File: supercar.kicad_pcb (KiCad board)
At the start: 2 copper layers, 63.5 x 48.9 mm, 59 parts, among them SW1 Power, U1 74HC283, U2 74HC574, U3 74HC154, U4 74HC574, U5 74HC21, U6 74HC02, U7 74HC04, U8 NE555D

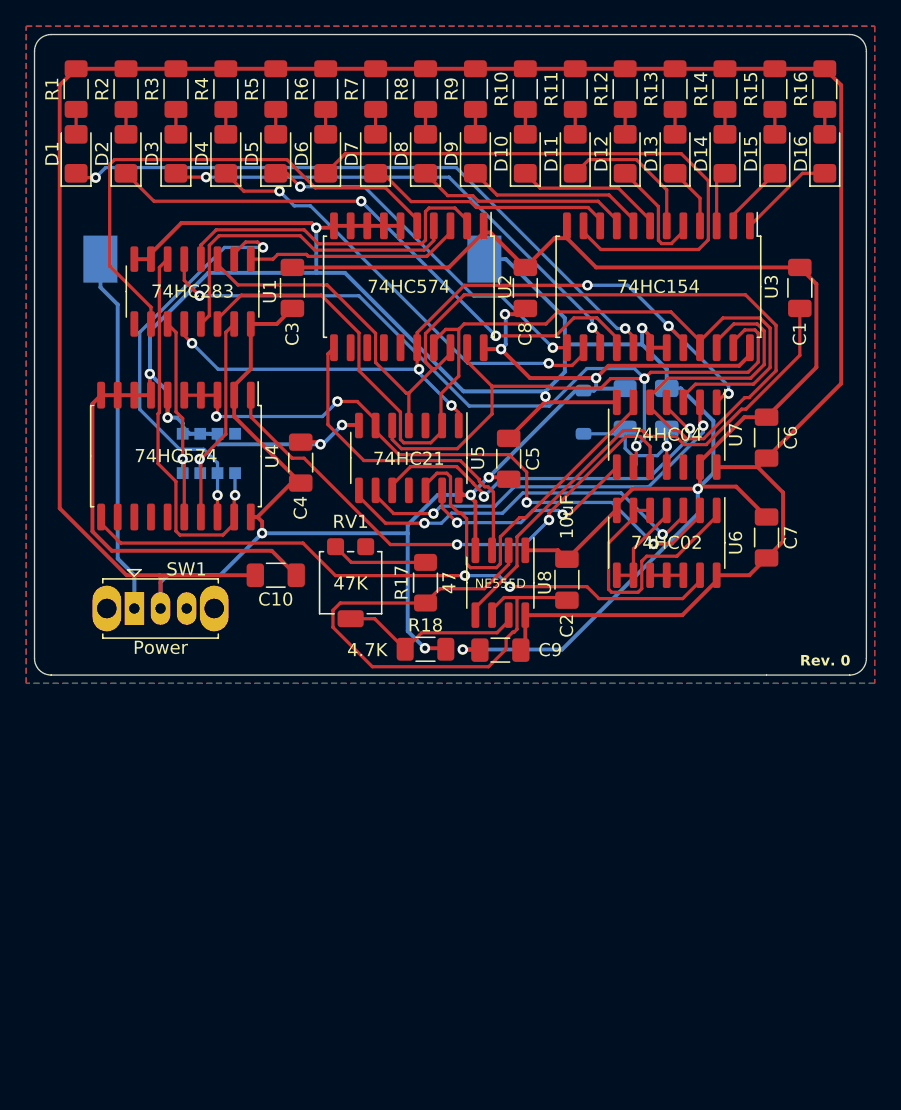
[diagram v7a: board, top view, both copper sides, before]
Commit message: Reduce IC count and reroute the board
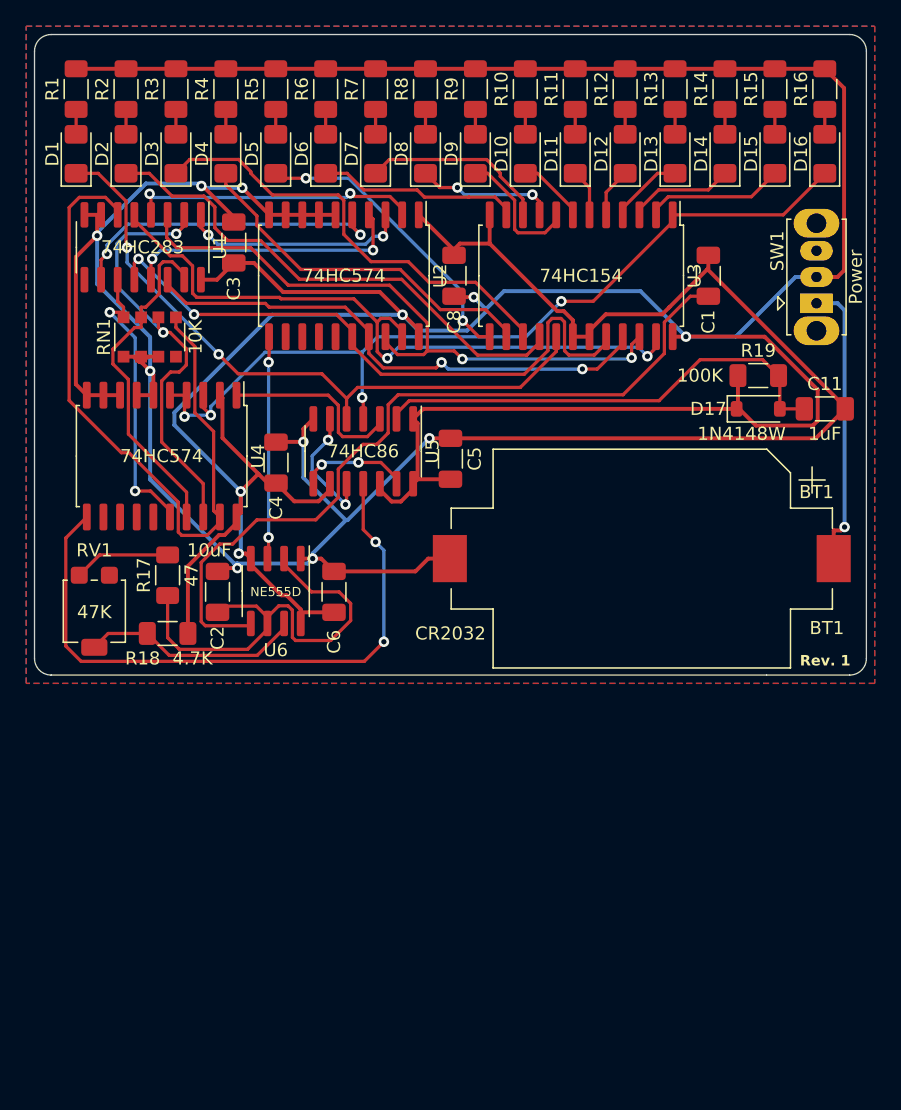
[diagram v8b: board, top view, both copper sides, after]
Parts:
- removed C10, C7, C9: 100nF, Capacitor_SMD:C_1206_3216Metric_Pad1.33x1.80mm_HandSolder
- removed the U6 at (126.4, 78.2)
- removed U7: 74HC04, Package_SO:SOIC-14_3.9x8.7mm_P1.27mm
- BT1, C11, D17, R19, RN1: moved to F.Cu
- U5: value 74HC21 -> 74HC86
- moved SW1 57.0 mm to (137.8, 59.9), turned to 90 degrees
- moved BT1 35.1 mm to (124.5, 79.4), turned to 180 degrees
- moved C6 35.1 mm to (101.0, 81.9)
- moved C2 26.7 mm to (92.1, 81.9)
- moved R18 19.7 mm to (88.3, 85.1)
- moved R17 19.7 mm to (88.3, 80.6)
- moved RV1 19.7 mm to (82.7, 83.4)
- moved U6 17.2 mm to (96.5, 81.8)
- moved D17 13.3 mm to (133.3, 67.9), turned to 0 degrees
- moved C11 12.1 mm to (138.4, 67.9), turned to 0 degrees
- moved R19 10.5 mm to (133.3, 65.4), turned to 180 degrees
- moved RN1 9.97 mm to (86.9, 62.5), turned to 90 degrees
- moved C1 7.05 mm to (129.5, 57.8)
- moved U3 5.96 mm to (119.8, 57.8)
- moved C3 5.66 mm to (93.3, 55.2)
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- renumbered U8 to U6
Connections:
- D1 pad 1: Net-(D1-K) -> /LAST_BIT
- D16 pad 1: Net-(D16-K) -> /FIRST_BIT
- U3 pad 1: Net-(D16-K) -> /FIRST_BIT
- U3 pad 17: Net-(D1-K) -> /LAST_BIT
- U4 pad 3: Net-(U4-D1) -> /FIRST_BIT
- U4 pad 4: Net-(U4-D1) -> /FIRST_BIT
- U4 pad 5: Net-(U4-D1) -> /FIRST_BIT
- U5 pad 1: Net-(U1-A4) -> +3V3
- U5 pad 11: (no net) -> Net-(U4-Cp)
- U5 pad 12: Net-(U5-Pad12) -> +3V3
- U5 pad 2: Net-(U1-A3) -> Net-(D17-A)
- U5 pad 3: (no net) -> /RST
- U5 pad 4: Net-(U1-A2) -> /FIRST_BIT
- U5 pad 5: Net-(U1-A1) -> /LAST_BIT
- U5 pad 6: Net-(U4-D1) -> Net-(U5-Pad10)
- U5 pad 8: Net-(U5-Pad8) -> Net-(U5-Pad13)
- U5 pad 9: Net-(U5-Pad9) -> +3V3
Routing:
- net GND: track 284.7 -> 205.9 mm, vias 9 -> 8
- net /FIRST_BIT: track 0.00 -> 67.1 mm, vias 0 -> 4
- net /LAST_BIT: track 0.00 -> 50.6 mm, vias 0 -> 2
- net Net-(U4-D1): track 49.3 -> 0.00 mm, vias 4 -> 0
- net Net-(D1-K): track 49.2 -> 0.00 mm, vias 2 -> 0
- net Net-(U1-A2): track 93.9 -> 48.4 mm, vias 0 -> 2
- net Net-(U1-A1): track 91.5 -> 51.7 mm, vias 3 -> 2
- net Net-(U1-A3): track 75.2 -> 40.5 mm, vias 0 -> 2
- net Net-(U5-Pad9): track 30.9 -> 0.00 mm, vias 2 -> 0
- net Net-(D6-K): track 46.1 -> 15.4 mm
- net Net-(U5-Pad12): track 29.7 -> 0.00 mm
- net Net-(U5-Pad8): track 29.4 -> 0.00 mm, vias 2 -> 0
- net /RST: track 41.8 -> 14.3 mm, vias 2 -> 0
- net Net-(D17-A): track 11.2 -> 36.2 mm, vias 1 -> 0
- net +3V3: track 293.4 -> 269.2 mm, vias 7 -> 5
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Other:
- board text added: "Rev. 1"
- board text removed: "Rev. 0"
